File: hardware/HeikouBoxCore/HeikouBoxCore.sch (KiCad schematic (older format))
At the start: 35 parts, among them J1 L, J2 B, J3 R, J4 T, U1 EP3C25E144

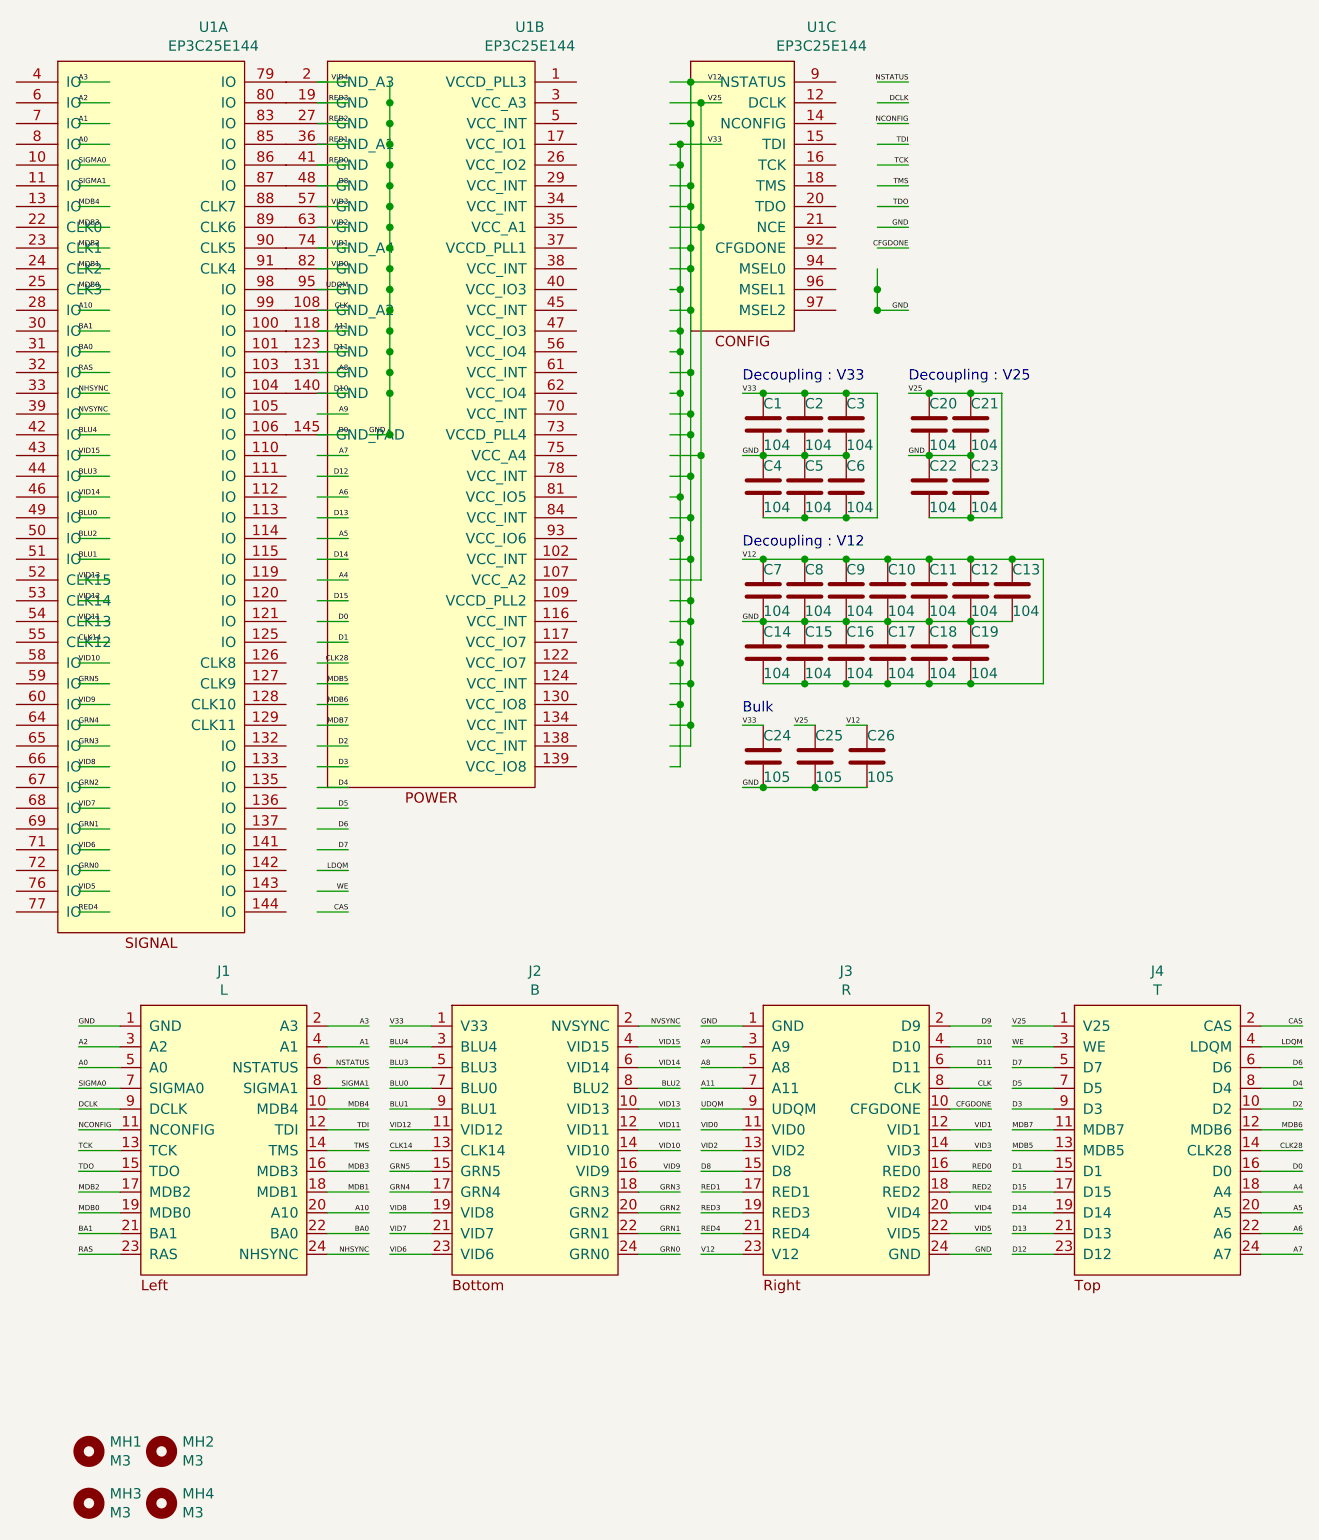
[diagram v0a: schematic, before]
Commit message: Core: Create/use overall footprint again
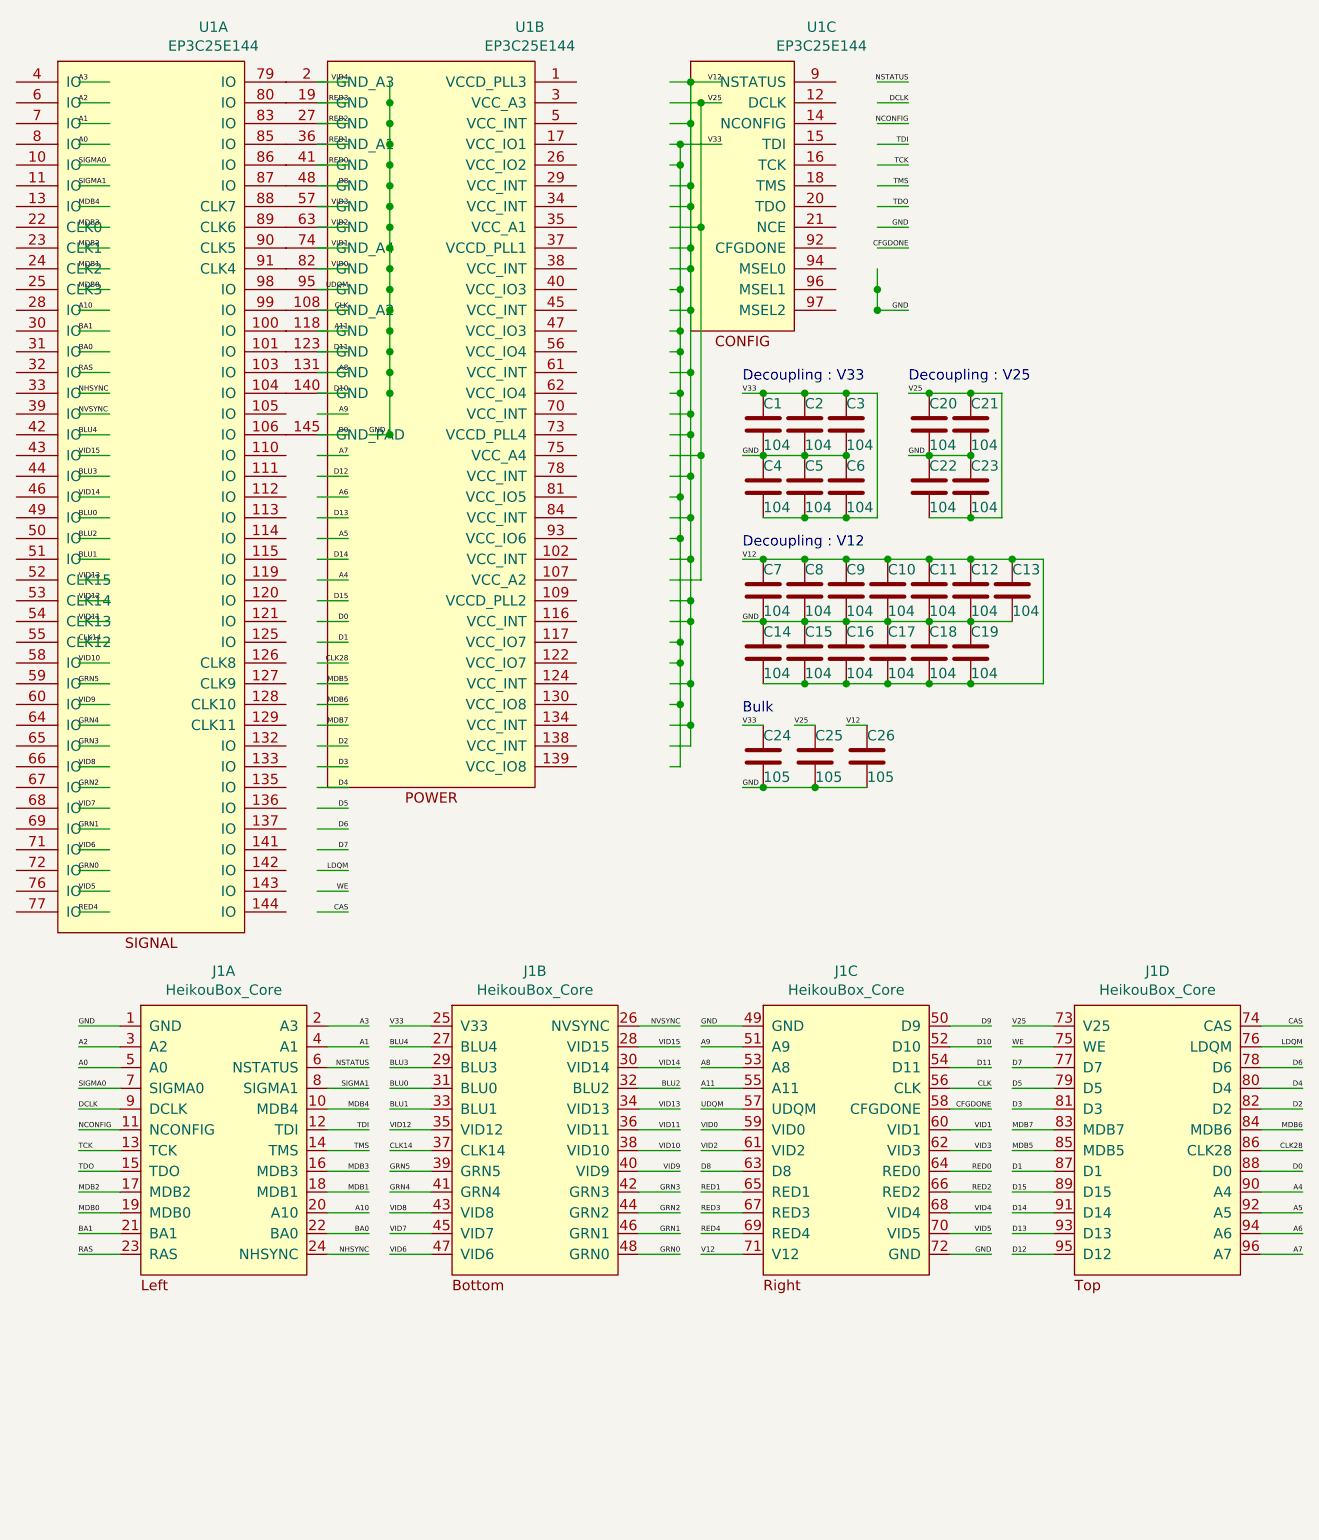
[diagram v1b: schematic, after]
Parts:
- removed J1: L, KSK_HeikouBox:PinHeader_2x12_P2.00mm_Vertical-MIRRORED, symbol KSK_HeikouBox:HeikouBox_Core_Conn_Left
- removed J2: B, KSK_HeikouBox:PinHeader_2x12_P2.00mm_Vertical-MIRRORED, symbol KSK_HeikouBox:HeikouBox_Core_Conn_Bottom
- removed J3: R, KSK_HeikouBox:PinHeader_2x12_P2.00mm_Vertical-MIRRORED, symbol KSK_HeikouBox:HeikouBox_Core_Conn_Right
- removed J4: T, KSK_HeikouBox:PinHeader_2x12_P2.00mm_Vertical-MIRRORED, symbol KSK_HeikouBox:HeikouBox_Core_Conn_Top
- removed MH1, MH2, MH3, MH4: M3, MountingHole:MountingHole_3.2mm_M3, symbol Mechanical:MountingHole
- added J1: HeikouBox_Core, KSK_HeikouBox:HeikouBox-Core-Top, symbol KSK_HeikouBox:HeikouBox_Core
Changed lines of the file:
@@
 	4400 1800 4400 1900
 $Comp
-L KSK_HeikouBox:HeikouBox_Core_Conn_Left J1
-U 1 1 5EF5786F
+L KSK_HeikouBox:HeikouBox_Core J1
+U 1 1 5FCEAF88
 P 850 5250
 F 0 "J1" H 1250 5415 50  0000 C CNN
-F 1 "L" H 1250 5324 50  0000 C CNN
-F 2 "KSK_HeikouBox:PinHeader_2x12_P2.00mm_Vertical-MIRRORED" H 1150 5250 50  0001 C CNN
+F 1 "HeikouBox_Core" H 1250 5324 50  0000 C CNN
+F 2 "KSK_HeikouBox:HeikouBox-Core-Top" H 1150 5250 50  0001 C CNN
 F 3 "" H 1150 5250 50  0001 C CNN
 	1    850  5250
@@
 $EndComp
 $Comp
-L KSK_HeikouBox:HeikouBox_Core_Conn_Top J4
-U 1 1 5EF57BDC
-P 5350 5250
-F 0 "J4" H 5750 5415 50  0000 C CNN
-F 1 "T" H 5750 5324 50  0000 C CNN
-F 2 "KSK_HeikouBox:PinHeader_2x12_P2.00mm_Vertical-MIRRORED" H 5650 5250 50  0001 C CNN
-F 3 "" H 5650 5250 50  0001 C CNN
-	1    5350 5250
+L KSK_HeikouBox:HeikouBox_Core J1
+U 2 1 5FCEF84D
+P 2350 5250
+F 0 "J1" H 2750 5415 50  0000 C CNN
+F 1 "HeikouBox_Core" H 2750 5324 50  0000 C CNN
+F 2 "KSK_HeikouBox:HeikouBox-Core-Top" H 2650 5250 50  0001 C CNN
+F 3 "" H 2650 5250 50  0001 C CNN
+	2    2350 5250
 	1    0    0    -1
 $EndComp
 $Comp
-L KSK_HeikouBox:HeikouBox_Core_Conn_Right J3
-U 1 1 5EF57CAD
+L KSK_HeikouBox:HeikouBox_Core J1
+U 3 1 5FCF1408
 P 3850 5250
-F 0 "J3" H 4250 5415 50  0000 C CNN
-F 1 "R" H 4250 5324 50  0000 C CNN
-F 2 "KSK_HeikouBox:PinHeader_2x12_P2.00mm_Vertical-MIRRORED" H 4150 5250 50  0001 C CNN
+F 0 "J1" H 4250 5415 50  0000 C CNN
+F 1 "HeikouBox_Core" H 4250 5324 50  0000 C CNN
+F 2 "KSK_HeikouBox:HeikouBox-Core-Top" H 4150 5250 50  0001 C CNN
 F 3 "" H 4150 5250 50  0001 C CNN
-	1    3850 5250
+	3    3850 5250
 	1    0    0    -1
 $EndComp
 $Comp
-L KSK_HeikouBox:HeikouBox_Core_Conn_Bottom J2
-U 1 1 5EF57D70
-P 2350 5250
-F 0 "J2" H 2750 5415 50  0000 C CNN
-F 1 "B" H 2750 5324 50  0000 C CNN
-F 2 "KSK_HeikouBox:PinHeader_2x12_P2.00mm_Vertical-MIRRORED" H 2650 5250 50  0001 C CNN
-F 3 "" H 2650 5250 50  0001 C CNN
-	1    2350 5250
+L KSK_HeikouBox:HeikouBox_Core J1
+U 4 1 5FCF324E
+P 5350 5250
+F 0 "J1" H 5750 5415 50  0000 C CNN
+F 1 "HeikouBox_Core" H 5750 5324 50  0000 C CNN
+F 2 "KSK_HeikouBox:HeikouBox-Core-Top" H 5650 5250 50  0001 C CNN
+F 3 "" H 5650 5250 50  0001 C CNN
+	4    5350 5250
 	1    0    0    -1
 $EndComp
-$Comp
-L Mechanical:MountingHole MH1
-U 1 1 5F54E1E3
-P 600 7400
-F 0 "MH1" H 700 7446 50  0000 L CNN
-F 1 "M3" H 700 7355 50  0000 L CNN
-F 2 "MountingHole:MountingHole_3.2mm_M3" H 600 7400 50  0001 C CNN
-F 3 "~" H 600 7400 50  0001 C CNN
-	1    600  7400
-	1    0    0    -1
-$EndComp
-$Comp
-L Mechanical:MountingHole MH2
-U 1 1 5F54F68B
-P 950 7400
-F 0 "MH2" H 1050 7446 50  0000 L CNN
-F 1 "M3" H 1050 7355 50  0000 L CNN
-F 2 "MountingHole:MountingHole_3.2mm_M3" H 950 7400 50  0001 C CNN
-F 3 "~" H 950 7400 50  0001 C CNN
-	1    950  7400
-	1    0    0    -1
-$EndComp
-$Comp
-L Mechanical:MountingHole MH3
-U 1 1 5F54F907
-P 600 7650
-F 0 "MH3" H 700 7696 50  0000 L CNN
-F 1 "M3" H 700 7605 50  0000 L CNN
-F 2 "MountingHole:MountingHole_3.2mm_M3" H 600 7650 50  0001 C CNN
-F 3 "~" H 600 7650 50  0001 C CNN
-	1    600  7650
-	1    0    0    -1
-$EndComp
-$Comp
-L Mechanical:MountingHole MH4
-U 1 1 5F54FB04
-P 950 7650
-F 0 "MH4" H 1050 7696 50  0000 L CNN
-F 1 "M3" H 1050 7605 50  0000 L CNN
-F 2 "MountingHole:MountingHole_3.2mm_M3" H 950 7650 50  0001 C CNN
-F 3 "~" H 950 7650 50  0001 C CNN
-	1    950  7650
-	1    0    0    -1
-$EndComp

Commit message: Update components on core
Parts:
- J1: value HeikouBox_Core -> HeikouBox-Core; symbol KSK_HeikouBox:HeikouBox_Core -> KSK_HeikouBox:HeikouBox-Core
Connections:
- wire segments 322 -> 321
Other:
- moved on the sheet: C1, C10, C11, C12, C13, C14, C15, C16, C17, C18, C19, C2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

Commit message: Mostly routed board
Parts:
- C1, C10, C11, C12, C13, C14, C15, C16, C17, C18, C19, C2, C20, C21, C22, C23, C3, C4, C5, C6, C7, C8, C9: value 104 -> 100n
- C24, C25, C26: value 105 -> 1u
- J1: value HeikouBox-Core -> HeikouBox-Core-Plug; symbol KSK_HeikouBox:HeikouBox-Core -> KSK_HeikouBox:HeikouBox-Core-Plug
- U1: footprint KSK_HeikouBox:EQFP-144-HANDSOLDER -> KSK_HeikouBox:LQFP-144-1EP_20x20mm_P0.5mm_EP6.61x6.61mm_HandSoldering
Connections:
- net GND: now also U1.94 (MSEL0)
- net V12 renamed 1V2
- net V25 renamed 2V5
- net V33 renamed 3V3
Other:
- note added: "Decoupling : 1V2"
- note added: "Decoupling : 2V5"
- note added: "Decoupling : 3V3"
- note removed: "Decoupling : V12"
- note removed: "Decoupling : V25"
- note removed: "Decoupling : V33"
- moved on the sheet: C1, C10, C11, C12, C13, C14, C15, C16, C17, C18, C19, C2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
